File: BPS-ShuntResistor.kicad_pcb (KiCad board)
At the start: 2 copper layers, 40.1 x 35.1 mm, 18 parts, among them J3 Amp_Conn

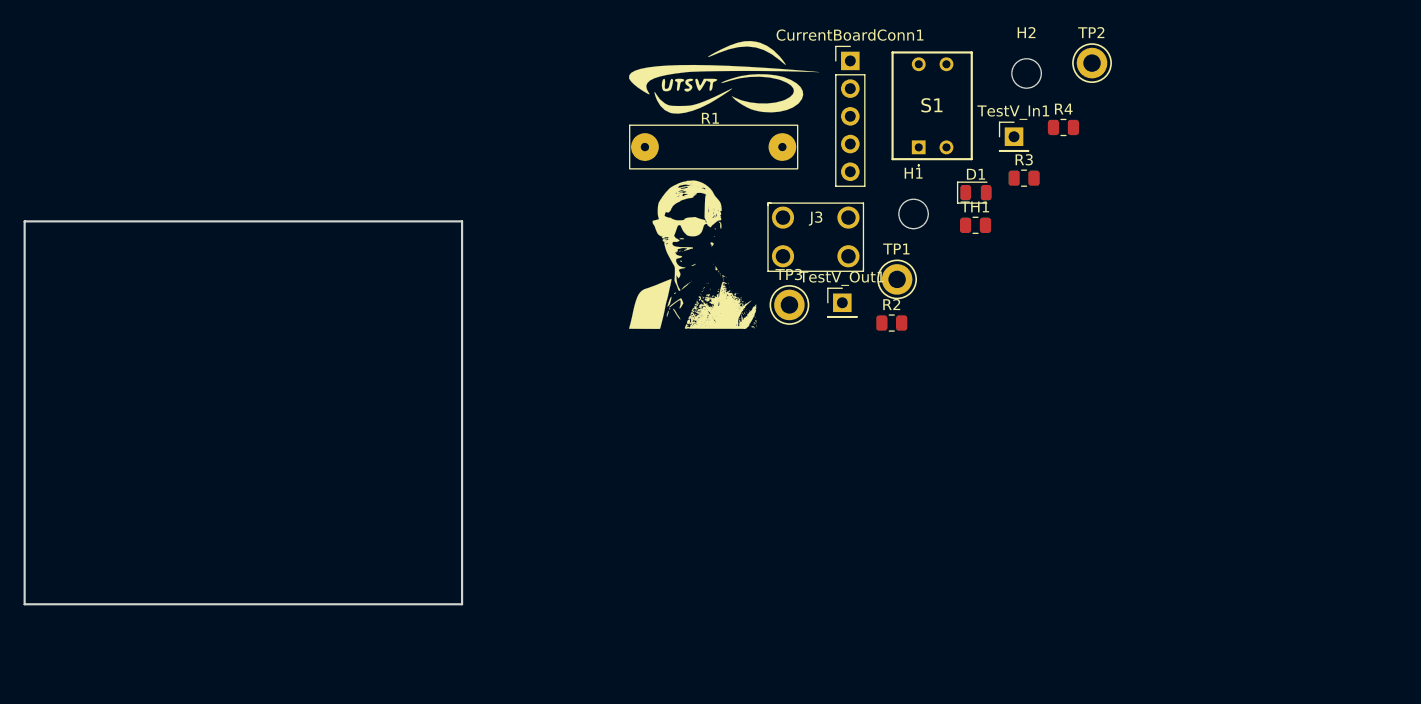
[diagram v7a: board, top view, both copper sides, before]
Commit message: reorganizing board
workign on sync between amp board and this one
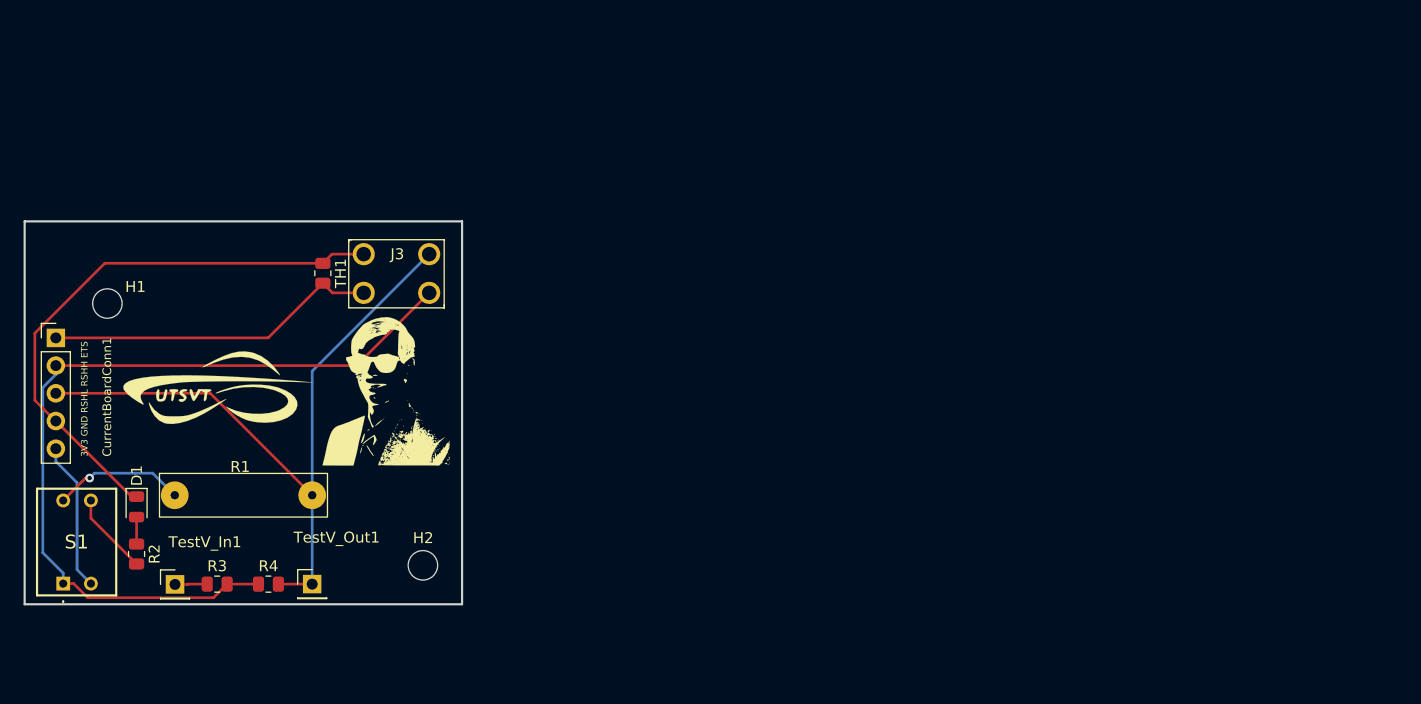
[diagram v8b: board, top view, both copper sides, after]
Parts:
- removed TP1, TP2, TP3: TestPoint, TestPoint:TestPoint_Keystone_5005-5009_Compact
- moved S1 88.0 mm to (112.0, 110.7)
- moved TestV_In1 87.2 mm to (122.3, 110.8)
- moved R4 84.1 mm to (130.8, 110.7)
- moved R3 82.8 mm to (126.1, 110.7)
- moved D1 82.2 mm to (118.8, 103.6), turned to -90 degrees
- moved CurrentBoardConn1 77.1 mm to (111.3, 88.2)
- moved H1 74.4 mm to (116.1, 85.0)
- moved R2 72.4 mm to (118.8, 108.0), turned to -90 degrees
- moved H2 71.4 mm to (145.0, 109.0)
- moved TH1 60.0 mm to (135.8, 82.2), turned to -90 degrees
- moved TestV_Out1 55.0 mm to (134.8, 110.7)
- moved LOGO1 54.4 mm to (126.0, 92.8)
- moved R1 53.6 mm to (128.2, 102.6)
- moved J3 38.6 mm to (142.6, 82.0)
- moved LOGO2 30.8 mm to (141.2, 92.9)
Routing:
- net RSHH: track 0.00 -> 77.2 mm
- net RSHL: track 0.00 -> 65.2 mm
- net GND: track 0.00 -> 52.3 mm
- net ETS: track 0.00 -> 30.7 mm
- net +3V3: track 0.00 -> 13.7 mm
- net Net-(R1-Pad1): track 0.00 -> 12.1 mm, vias 0 -> 1
- net Net-(R2-Pad2): track 0.00 -> 7.55 mm
- net Net-(R3-Pad1): track 0.00 -> 2.96 mm
- net Net-(D1-Pad2): track 0.00 -> 2.47 mm
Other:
- board text added: "3V3 GND RSHL RSHH ETS"
